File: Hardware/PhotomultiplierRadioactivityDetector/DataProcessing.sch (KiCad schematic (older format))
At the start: 22 parts, among them J1 Conn_01x04, J15 Conn_01x02_Female, J2 Conn_02x05_Counter_Clockwise, U2 STM8S003F3P

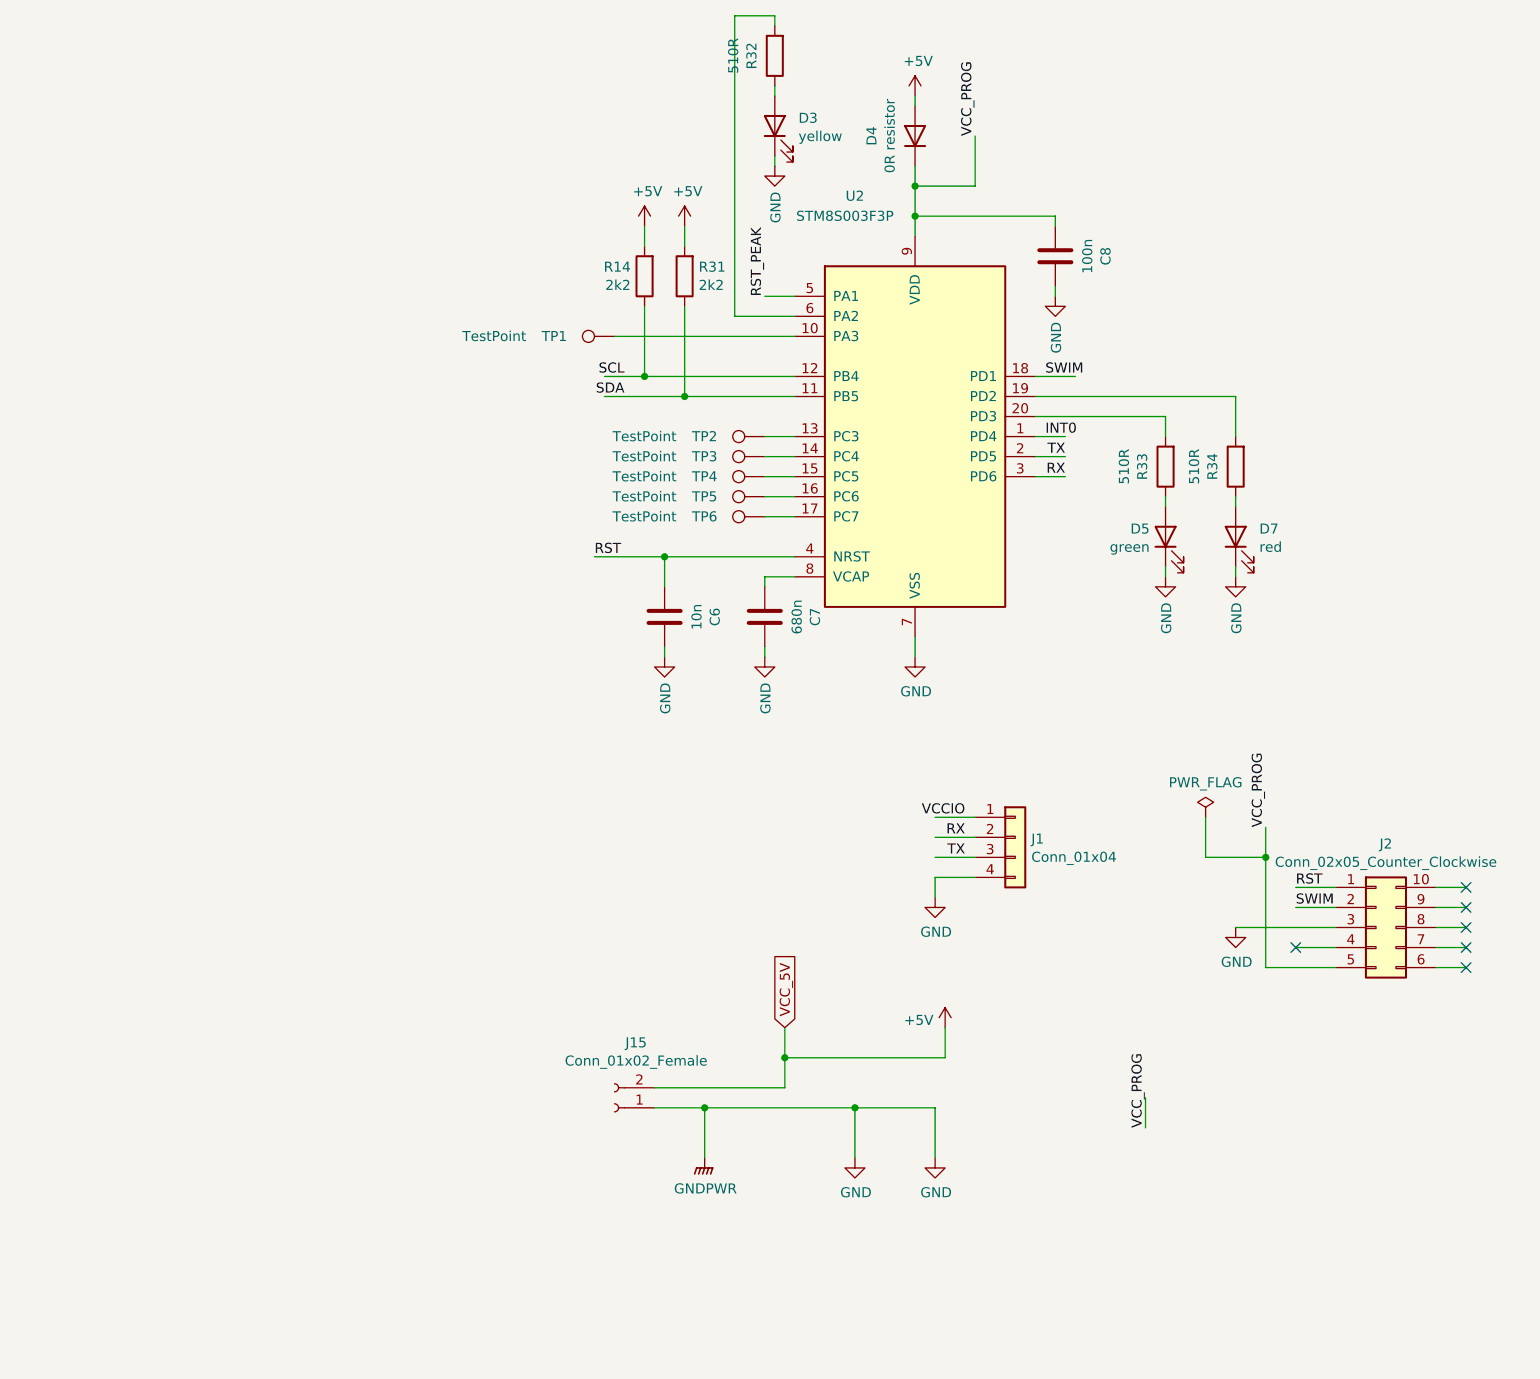
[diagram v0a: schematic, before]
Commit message: draft of hw power supply
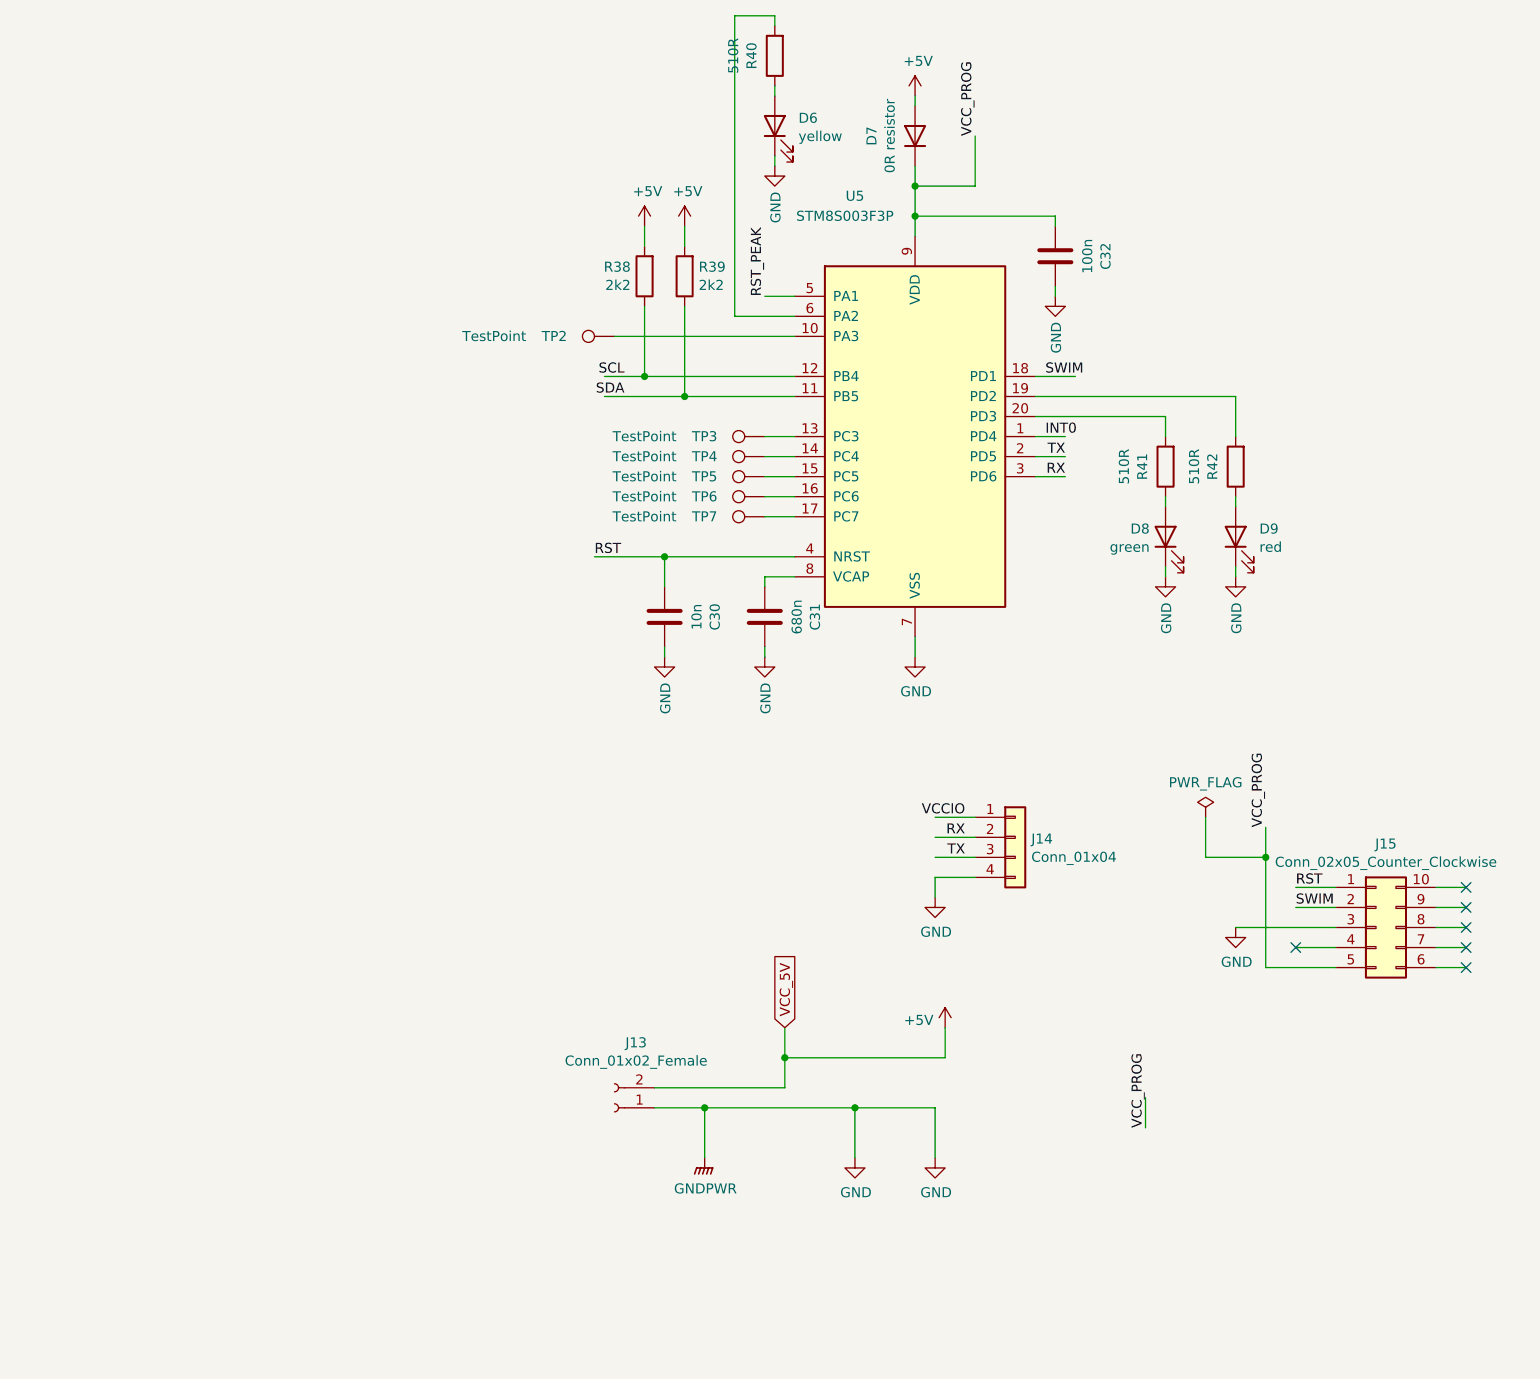
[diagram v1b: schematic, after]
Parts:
- renumbered C6 to C30, C7 to C31, C8 to C32, D3 to D6, D4 to D7, D5 to D8, D7 to D9, J15 to J13, J1 to J14, J2 to J15, R14 to R38, R31 to R39, R32 to R40, R33 to R41, R34 to R42, TP1 to TP2, TP2 to TP3, TP3 to TP4, TP4 to TP5, TP5 to TP6, TP6 to TP7, U2 to U5

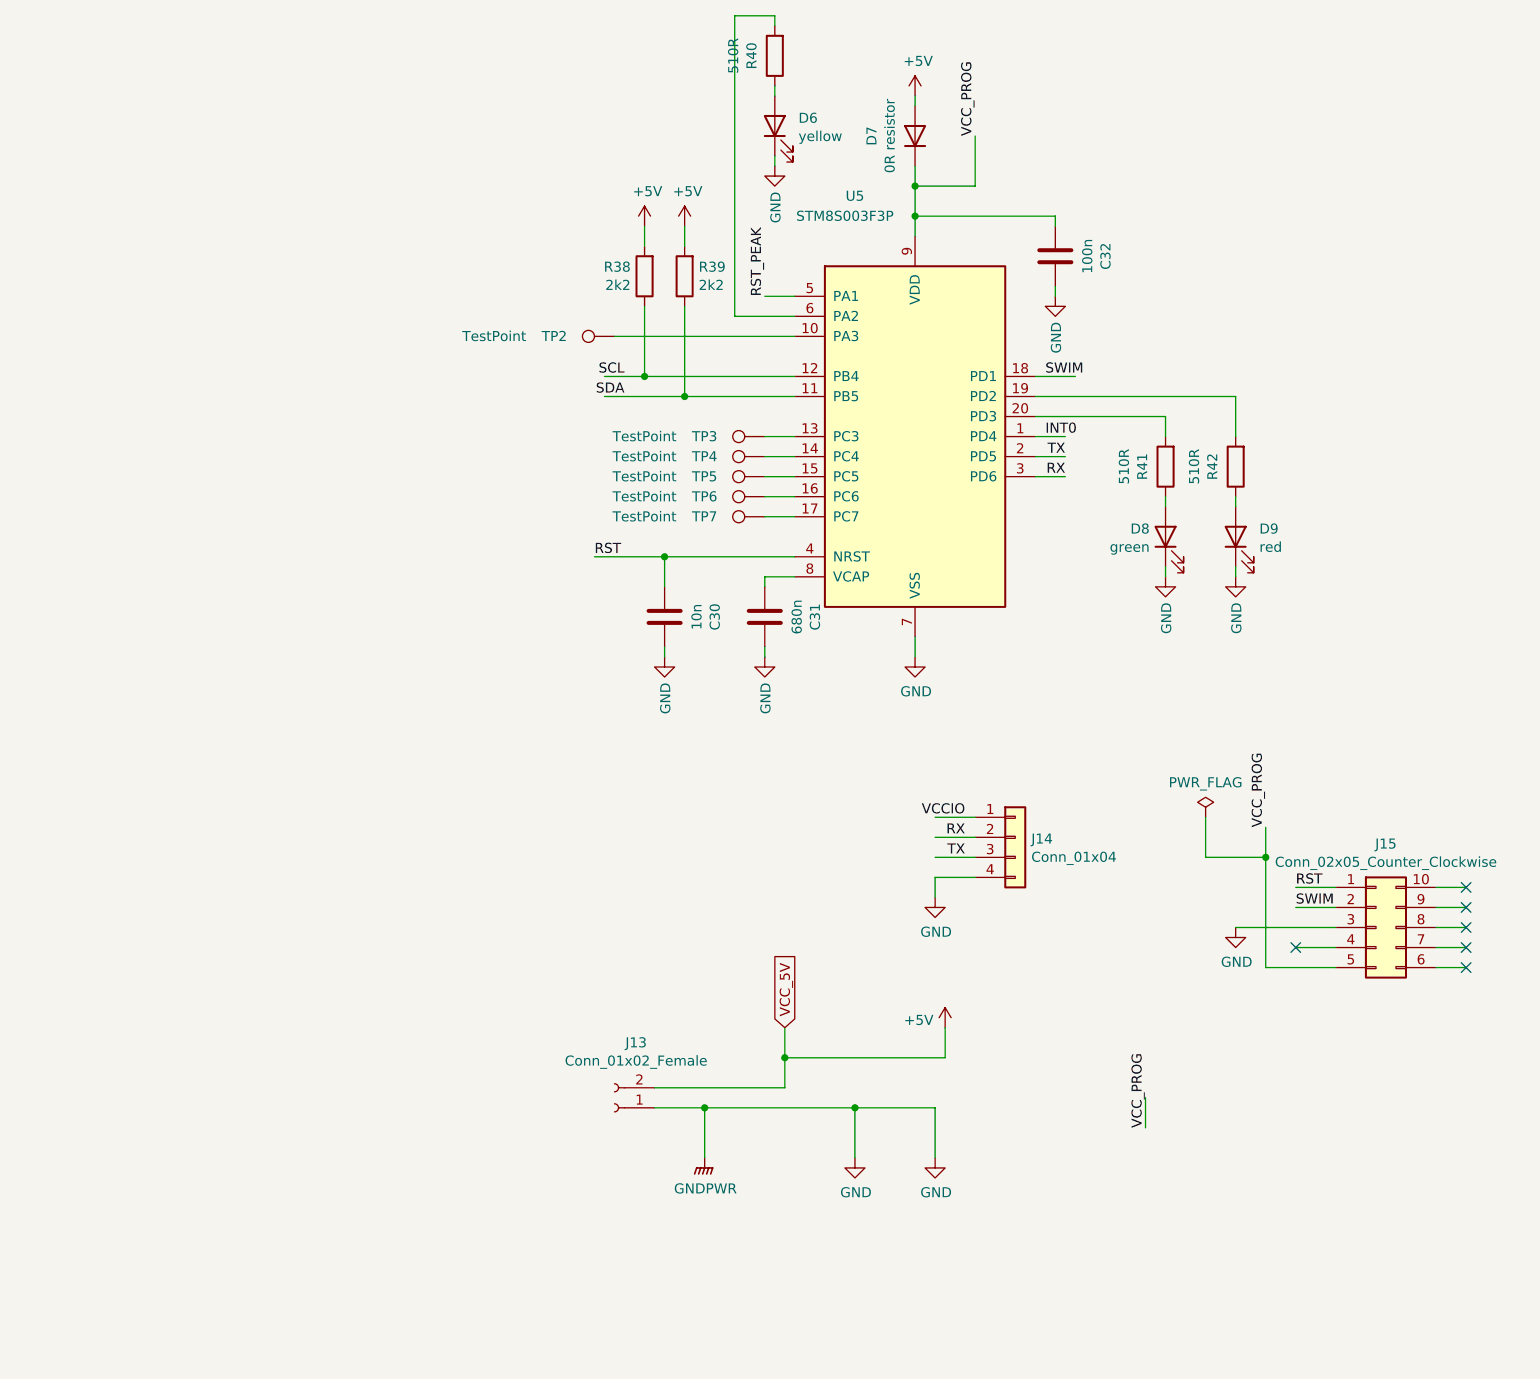
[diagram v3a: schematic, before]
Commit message: upgarte mcu
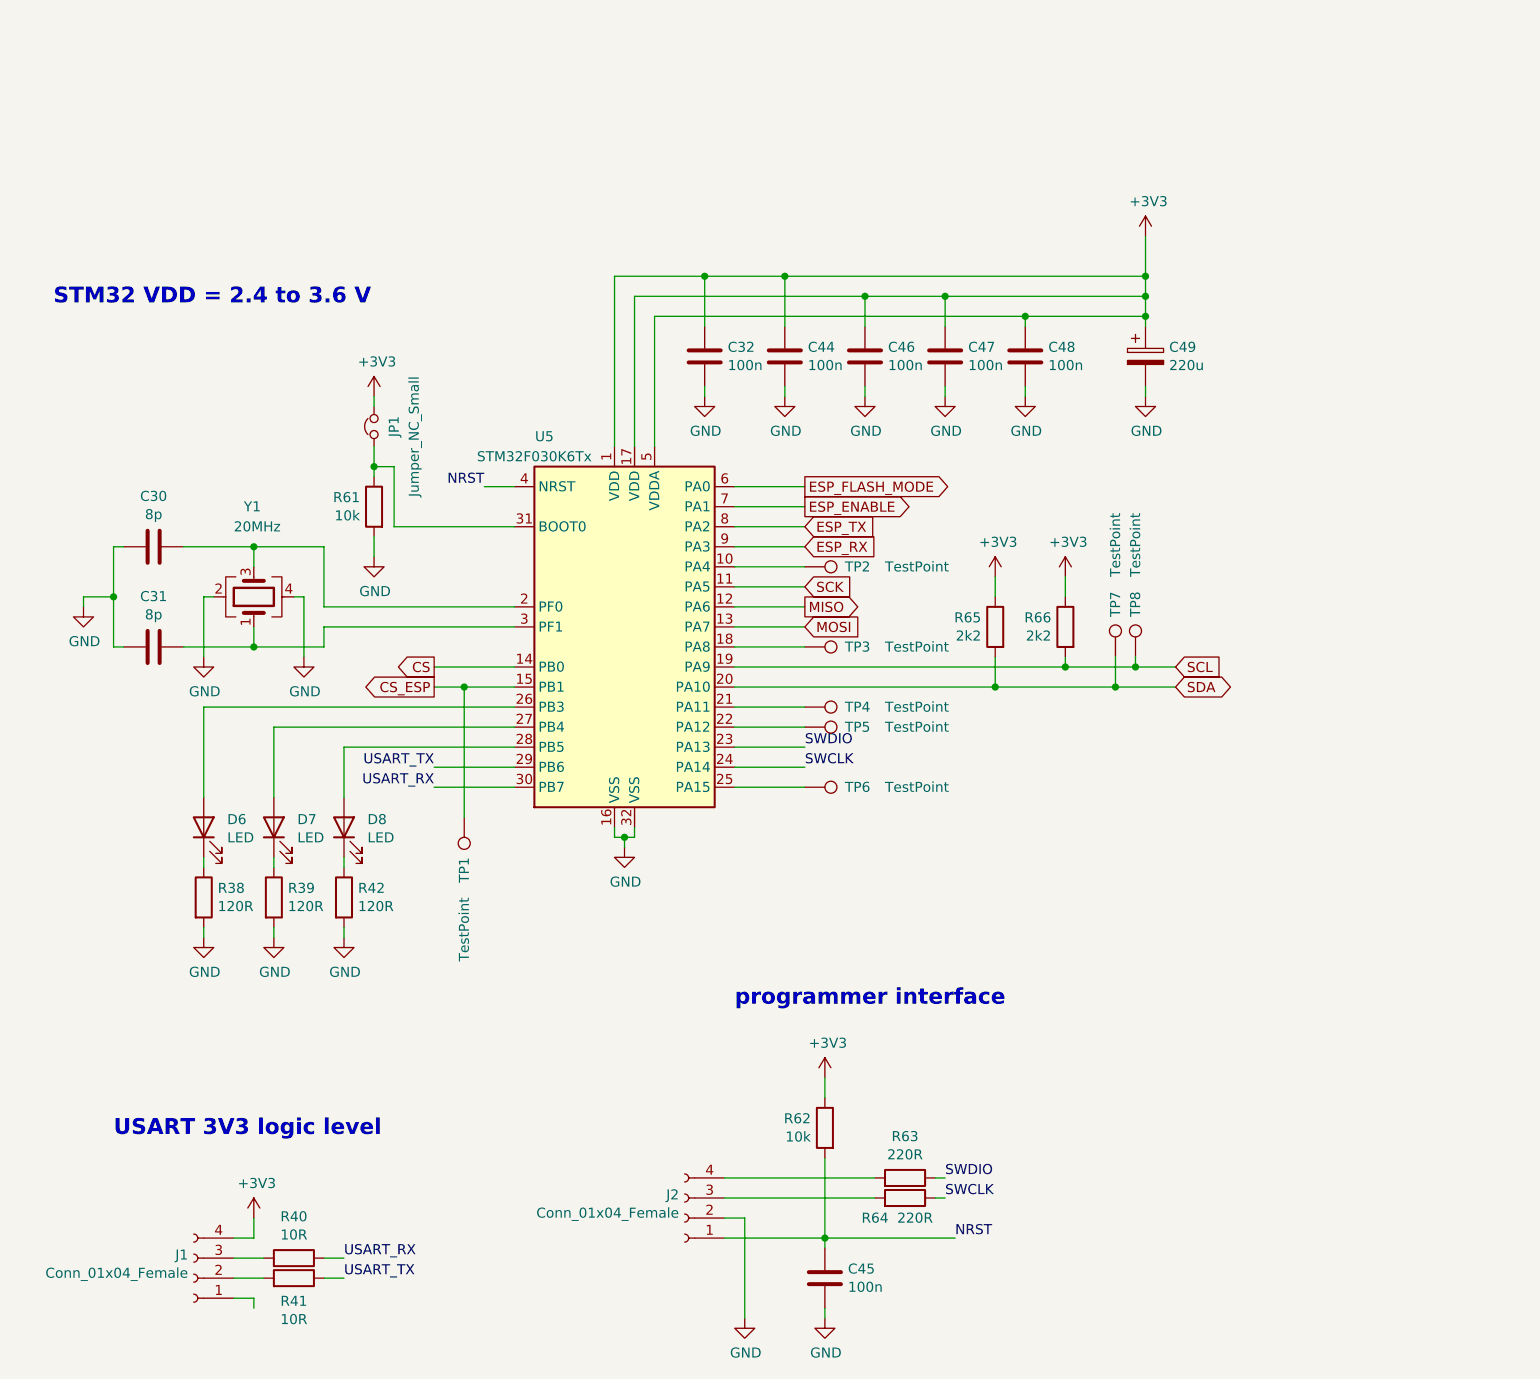
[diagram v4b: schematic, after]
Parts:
- removed D7: 0R resistor, Diode_SMD:D_MiniMELF, symbol Device:D
- removed D9: red, LED_SMD:LED_0805_2012Metric, symbol Device:LED
- removed J13: Conn_01x02_Female, Connector_PinHeader_2.54mm:PinHeader_2x01_P2.54mm_Vertical, symbol Connector:Conn_01x02_Female
- removed J14: Conn_01x04, Connector_PinSocket_2.54mm:PinSocket_1x04_P2.54mm_Horizontal, symbol Connector_Generic:Conn_01x04
- removed J15: Conn_02x05_Counter_Clockwise, Connector_PinSocket_2.54mm:PinSocket_2x05_P2.54mm_Horizontal, symbol Connector_Generic:Conn_02x05_Counter_Clockwise
- removed U5: STM8S003F3P, Package_SO:TSSOP-20_4.4x6.5mm_P0.65mm, symbol MCU_ST_STM8:STM8S003F3P
- added C44, C45, C46, C47, C48: 100n, Capacitor_SMD:C_0805_2012Metric_Pad1.15x1.40mm_HandSolder, symbol Device:C
- added C49: 220u, Capacitor_SMD:CP_Elec_6.3x5.8, symbol Device:CP
- added D7: LED, LED_SMD:LED_0402_1005Metric, symbol Device:LED
- added J1, J2: Conn_01x04_Female, Connector_PinHeader_2.54mm:PinHeader_1x04_P2.54mm_Vertical, symbol Connector:Conn_01x04_Female
- added JP1: Jumper_NC_Small, Jumper:SolderJumper-2_P1.3mm_Bridged2Bar_RoundedPad1.0x1.5mm, symbol Device:Jumper_NC_Small
- added R61, R62: 10k, Resistor_SMD:R_0805_2012Metric_Pad1.15x1.40mm_HandSolder, symbol Device:R
- added R63, R64: 220R, Resistor_SMD:R_0805_2012Metric_Pad1.15x1.40mm_HandSolder, symbol Device:R
- added R65, R66: 2k2, Resistor_SMD:R_0805_2012Metric_Pad1.15x1.40mm_HandSolder, symbol Device:R
- added TP1, TP8: TestPoint, TestPoint:TestPoint_Pad_D1.0mm, symbol Connector:TestPoint
- added U5: STM32F030K6Tx, Package_QFP:LQFP-32_7x7mm_P0.8mm, symbol MCU_ST_STM32F0:STM32F030K6Tx
- added Y1: 20MHz, Oscillator:Oscillator_SMD_EuroQuartz_XO53-4Pin_5.0x3.2mm, symbol Device:Crystal_GND24
- C30: value 10n -> 8p
- C31: value 680n -> 8p
- D6: value yellow -> LED; footprint LED_SMD:LED_0805_2012Metric -> LED_SMD:LED_0402_1005Metric
- D8: value green -> LED; footprint LED_SMD:LED_0805_2012Metric -> LED_SMD:LED_0402_1005Metric
- R38, R39: value 2k2 -> 120R
- R40, R41: value 510R -> 10R
- R42: value 510R -> 120R
- TP2, TP3, TP4, TP5, TP6, TP7: footprint TestPoint:TestPoint_THTPad_1.0x1.0mm_Drill0.5mm -> TestPoint:TestPoint_Pad_D1.0mm
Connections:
- net labels added: +3V3, CS, CS_ESP, ESP_ENABLE, ESP_FLASH_MODE, ESP_RX, ESP_TX, MISO, MOSI, NRST, SCK, SWCLK, SWDIO, USART_RX, USART_TX
- net labels removed: +5V, GNDPWR, INT0, RST, RST_PEAK, RX, SWIM, TX, VCCIO, VCC_5V, VCC_PROG
- wire segments 81 -> 123
- no-connect marks 6 -> 0
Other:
- note added: "STM32 VDD = 2.4 to 3.6 V"
- note added: "USART 3V3 logic level"
- note added: "programmer interface"

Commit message: placement of components for hw generator
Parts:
- D6, D7, D8: footprint LED_SMD:LED_0402_1005Metric -> LED_SMD:LED_0805_2012Metric
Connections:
- net labels added: HV_EN
- net labels removed: ESP_ENABLE, ESP_FLASH_MODE, ESP_RX, ESP_TX
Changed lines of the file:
@@
 Wire Wire Line
 	2400 3050 2400 3100
-Text GLabel 4550 3250 2    50   Output ~ 0
-ESP_ENABLE
-Text GLabel 4550 3150 2    50   Output ~ 0
-ESP_FLASH_MODE
-Text GLabel 4550 3350 2    50   Input ~ 0
-ESP_TX
-Text GLabel 4550 3450 2    50   Input ~ 0
-ESP_RX
 Text GLabel 2700 4150 0    50   Output ~ 0
 CS_ESP
@@
 F 0 "D6" V 1589 4733 50  0000 R CNN
 F 1 "LED" V 1498 4733 50  0000 R CNN
-F 2 "LED_SMD:LED_0402_1005Metric" H 1550 4850 50  0001 C CNN
+F 2 "LED_SMD:LED_0805_2012Metric" H 1550 4850 50  0001 C CNN
 F 3 "~" H 1550 4850 50  0001 C CNN
 	1    1550 4850
@@
 F 0 "D7" V 1939 4733 50  0000 R CNN
 F 1 "LED" V 1848 4733 50  0000 R CNN
-F 2 "LED_SMD:LED_0402_1005Metric" H 1900 4850 50  0001 C CNN
+F 2 "LED_SMD:LED_0805_2012Metric" H 1900 4850 50  0001 C CNN
 F 3 "~" H 1900 4850 50  0001 C CNN
 	1    1900 4850
@@
 F 0 "D8" V 2289 4733 50  0000 R CNN
 F 1 "LED" V 2198 4733 50  0000 R CNN
-F 2 "LED_SMD:LED_0402_1005Metric" H 2250 4850 50  0001 C CNN
+F 2 "LED_SMD:LED_0805_2012Metric" H 2250 4850 50  0001 C CNN
 F 3 "~" H 2250 4850 50  0001 C CNN
 	1    2250 4850
@@
 	1    0    0    -1
 $EndComp
+Text GLabel 4550 3150 2    50   Output ~ 0
+HV_EN
 $EndSCHEMATC
